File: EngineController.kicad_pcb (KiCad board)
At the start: 4 copper layers, 50 x 100 mm, 239 parts, among them IC1 TPS61089RNRR, IC2 AP2205-W5-7, IC3 AP2205-W5-7, IC4 TPS61089RNRR, J1 RBUS, J10 Conn_01x02_Male, J11 1053131104, J12 1053131104, J13 1053131104, J2 USB_C_Receptacle_USB2.0, J3 ServoCH1, J4 ServoCH2, J5 1053131104, J6 1053131104, J7 1053131104, J8 GPIO Breakout, J9 Micro_SD_Card_Det, Q1 SSM3K15AMFV,L3F, Q2 BUK9M11-40EX, U1 ESP32-S3, U2 SN65HVD230, U3 LM66200DRLR, U4 MAX77827AEFD+T, U5 SC4215, U6 SiC437BED-T1-GE3, U7 LTV-247, U8 ADS131M06IPBS, Y1 R940000171

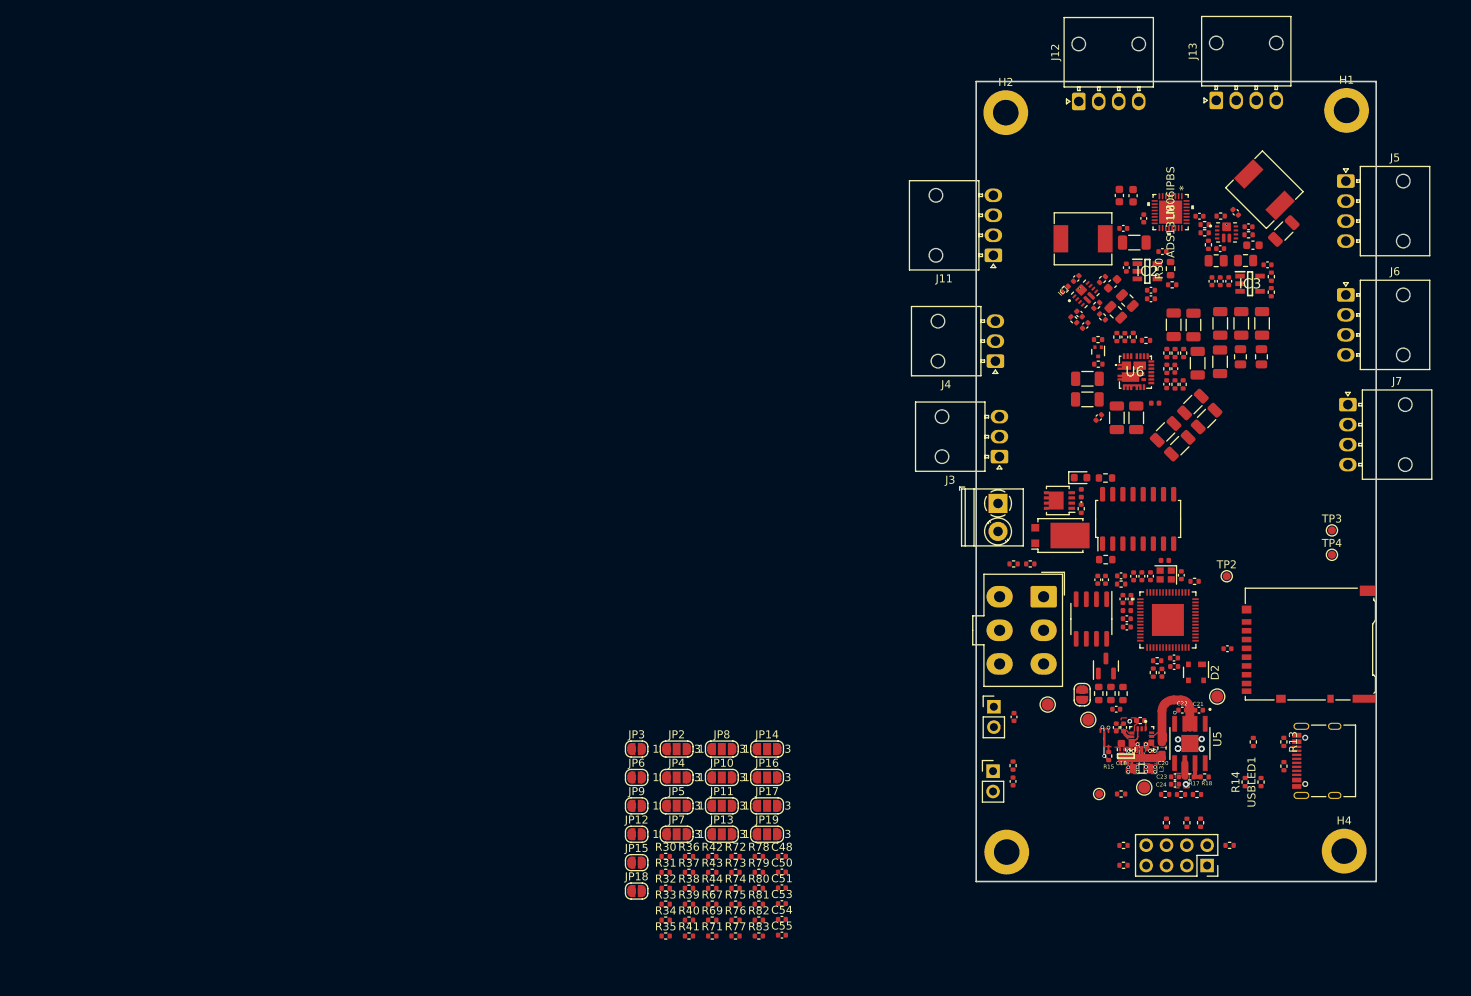
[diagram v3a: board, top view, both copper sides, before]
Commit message: Schematic done, components layed out, sensors wired up
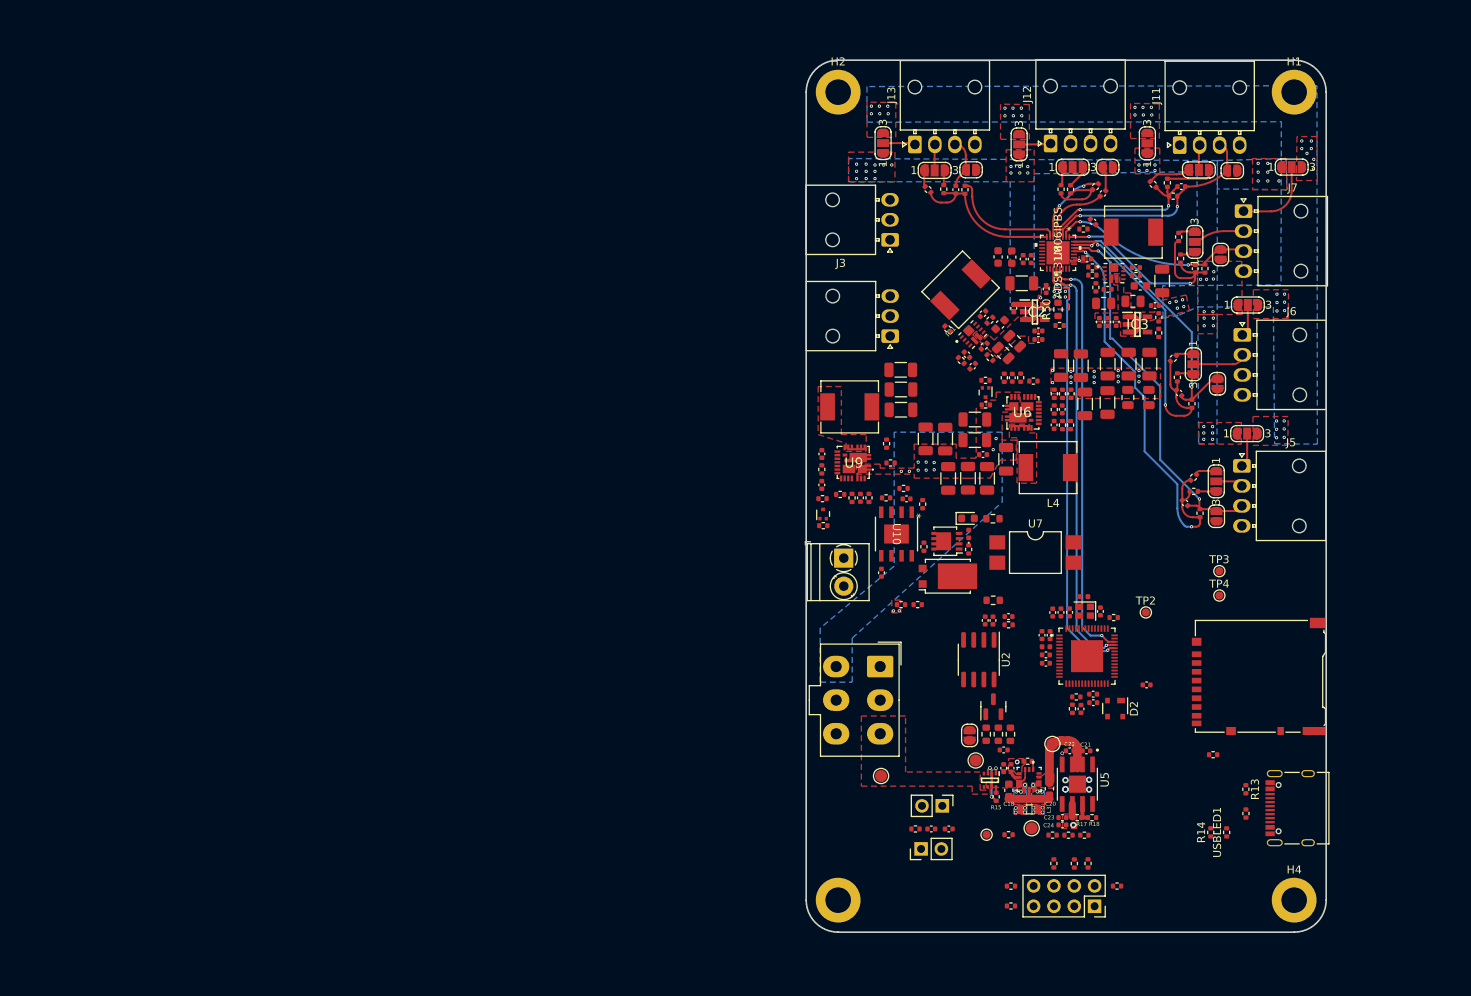
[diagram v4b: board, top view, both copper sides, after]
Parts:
- removed R71, R81, R82: 1k, Resistor_SMD:R_0402_1005Metric
- removed R80: 40.2k, Resistor_SMD:R_0402_1005Metric
- removed R83: 49k, Resistor_SMD:R_0402_1005Metric
- added C68: 1uF, Capacitor_SMD:C_0402_1005Metric, F.Cu at (137.9, 84.7)
- added C70: 4.7uF, Capacitor_SMD:C_0402_1005Metric, F.Cu at (137.9, 80.8)
- added C85: 47uF, Capacitor_SMD:C_1206_3216Metric, F.Cu at (147.8, 72.8)
- added C87: 47uF, Capacitor_SMD:C_1206_3216Metric, F.Cu at (147.8, 75.3)
- added C89: 47uF, Capacitor_SMD:C_1206_3216Metric, F.Cu at (147.7, 70.3)
- added C91: 0.1uF, Capacitor_SMD:C_0402_1005Metric, F.Cu at (142.7, 86.3)
- added C92: 2.2nF, Capacitor_SMD:C_0402_1005Metric, F.Cu at (148.5, 86.4)
- added C93: 100uF, Capacitor_SMD:C_0402_1005Metric, F.Cu at (145.3, 95.7)
- added L7: 3.3uH, iclr:IND_SRP6540-390M, F.Cu at (141.4, 74.9)
- added Q3: SSM3K15AMFV,L3F, Package_TO_SOT_SMD:SOT-723, F.Cu at (138.0, 88.3)
- added R52: 90k, Resistor_SMD:R_0402_1005Metric, F.Cu at (153.1, 47.7)
- added R53: 31.7k, Resistor_SMD:R_0402_1005Metric, F.Cu at (151.2, 47.8)
- added R54: 10k, Resistor_SMD:R_0402_1005Metric, F.Cu at (155.8, 47.8)
- added R57: 10k, Resistor_SMD:R_0402_1005Metric, F.Cu at (137.9, 82.7)
- added R58: 190k, Resistor_SMD:R_0402_1005Metric, F.Cu at (146.0, 79.5)
- added U10: TPS259621DDAT, EFuse:SO-PP-DDA-8_TEX, F.Cu at (147.2, 90.8)
- added U9: SiC437BED-T1-GE3, iclr:SiC437BEDT1GE3, F.Cu at (141.8, 81.9)
- C56: value 10uF -> 2.2uF
- C58: value 3.9nF -> 4.7nF
- L4: footprint Inductor_SMD:L_0402_1005Metric -> iclr:IND_SRP6540-390M
- R30: value 113k -> 90k
- R31: value 40.2k -> 31.7k
- R32, R38: value 1k -> 10k
- R33, R42: value 1k -> 90k
- R34: value 49k -> 31.7k
- R35, R67: value 113k -> 10k
- R36: value 40.2k -> 90k
- R37, R43: value 1k -> 31.7k
- R39: value 49k -> 90k
- R40: value 113k -> 31.7k
- R41, R75: value 40.2k -> 10k
- R44: value 49k -> 10k
- R45: value 7.87k -> 17.4k
- R46: value 360k -> 1K
- R47: value 100k -> 10k
- R48: value 560k -> 127k
- R51: value 309k -> 301k
- R56: value 360k -> 0k
- R69: value 40.2k -> 2.2
- R73: value 49k -> 200k
- R74: value 113k -> 100k
- R76: value 1k -> 464K
- R77: value 1k -> 33.2K
- R78: value 49k -> 47.5K
- R79: value 113k -> 453
- R85: value 953k -> 2k
- R86: value 118k -> 10k
- U7: footprint Package_SO:SOP-16_4.4x10.4mm_P1.27mm -> Package_DIP:SMDIP-4_W9.53mm
- moved JP12 111.5 mm to (189.2, 45.4), turned to 180 degrees
- moved R41 110.5 mm to (181.8, 48.6)
- moved R40 108.7 mm to (179.3, 47.1), turned to -45 degrees
- moved R39 108.2 mm to (181.1, 46.9), turned to -90 degrees
- moved JP15 105.0 mm to (173.6, 45.0), turned to 180 degrees
- moved JP10 104.4 mm to (196.6, 45.0)
- moved C53 102.6 mm to (182.8, 47.4)
- moved JP13 101.4 mm to (178.6, 42.0), turned to 90 degrees
- moved R38 100.8 mm to (185.8, 57.6), turned to 90 degrees
- moved JP9 100.4 mm to (187.7, 55.9), turned to 90 degrees
- moved R44 99.9 mm to (172.1, 47.4), turned to 45 degrees
- moved JP11 99.4 mm to (185.0, 45.3)
- moved JP18 99.4 mm to (156.5, 45.3), turned to 180 degrees
- moved C54 99.2 mm to (173.0, 48.2), turned to 45 degrees
- moved R36 98.7 mm to (182.5, 53.7), turned to -90 degrees
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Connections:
- net /Boosts/LDO11V_IN renamed /Boosts/LDO12V_IN
- C48 pad 1: /pressure_sensor/AIN3P -> /pressure_sensor/AIN0P
- C48 pad 2: /pressure_sensor/AIN3N -> /pressure_sensor/AIN0N
- C50 pad 1: /pressure_sensor/AIN4P -> /pressure_sensor/AIN1P
- C50 pad 2: /pressure_sensor/AIN4N -> /pressure_sensor/AIN1N
- C51 pad 1: /pressure_sensor/AIN5P -> /pressure_sensor/AIN2P
- C51 pad 2: /pressure_sensor/AIN5N -> /pressure_sensor/AIN2N
- C53 pad 1: /pressure_sensor/AIN0P -> /pressure_sensor/AIN3P
- C53 pad 2: /pressure_sensor/AIN0N -> /pressure_sensor/AIN3N
- C54 pad 1: /pressure_sensor/AIN2P -> /pressure_sensor/AIN4P
- C54 pad 2: /pressure_sensor/AIN2N -> /pressure_sensor/AIN4N
- C55 pad 1: /pressure_sensor/AIN1P -> /pressure_sensor/AIN5P
- C55 pad 2: /pressure_sensor/AIN1N -> /pressure_sensor/AIN5N
- C72 pad 2: Net-(U8-DVDD) -> +3V3
- C73 pad 1: /Boosts/10V -> +12V
- IC3 pad 5: /Boosts/10V -> +12V
- J10 pad 1: /Pyro/DeployPWR -> /Pyro/PyroV
- J6 pad 3: /pressure_sensor/AIN2N -> /pressure_sensor/AIN1N
- J7 pad 3: /pressure_sensor/AIN1N -> /pressure_sensor/AIN2N
- JP11 pad 3: /pressure_sensor/AIN3P -> Net-(JP11-B)
- JP14 pad 3: /pressure_sensor/AIN4P -> Net-(JP14-B)
- JP17 pad 3: /pressure_sensor/AIN5P -> Net-(JP17-B)
- JP2 pad 3: /pressure_sensor/AIN0P -> Net-(JP2-B)
- JP5 pad 3: /pressure_sensor/AIN2P -> Net-(JP5-B)
- JP6 pad 2: /pressure_sensor/AIN2N -> /pressure_sensor/AIN1N
- JP8 pad 3: /pressure_sensor/AIN1P -> Net-(JP8-B)
- JP9 pad 2: /pressure_sensor/AIN1N -> /pressure_sensor/AIN2N
- Q1 pad 1: /BUCK_EN -> /buckC/BUCKC_EN
- R24 pad 2: /BUCK_EN -> /buckC/BUCKC_EN
- R30 pad 1: Net-(R30-Pad1) -> Net-(JP2-B)
- R30 pad 2: Net-(R30-Pad2) -> /pressure_sensor/AIN0P
- R31 pad 1: Net-(R30-Pad2) -> Net-(JP2-A)
- R31 pad 2: Net-(R31-Pad2) -> /pressure_sensor/AIN0P
- R32 pad 1: Net-(R30-Pad1) -> /pressure_sensor/AIN0P
- R32 pad 2: /pressure_sensor/AIN0P -> /pressure_sensor/AIN0N
- R33 pad 1: Net-(R31-Pad2) -> Net-(JP5-B)
- R33 pad 2: Net-(JP2-A) -> /pressure_sensor/AIN1P
- R34 pad 1: /pressure_sensor/AIN0P -> Net-(JP5-A)
- R34 pad 2: /pressure_sensor/AIN0N -> /pressure_sensor/AIN1P
- R35 pad 1: Net-(R35-Pad1) -> /pressure_sensor/AIN1P
- R35 pad 2: Net-(R35-Pad2) -> /pressure_sensor/AIN1N
- R36 pad 1: Net-(R35-Pad2) -> Net-(JP8-B)
- R36 pad 2: Net-(R36-Pad2) -> /pressure_sensor/AIN2P
- R37 pad 1: Net-(R35-Pad1) -> Net-(JP8-A)
- R38 pad 1: Net-(R36-Pad2) -> /pressure_sensor/AIN2P
- R38 pad 2: Net-(JP5-A) -> /pressure_sensor/AIN2N
- R39 pad 1: /pressure_sensor/AIN2P -> Net-(JP11-B)
- R39 pad 2: /pressure_sensor/AIN2N -> /pressure_sensor/AIN3P
- R40 pad 1: Net-(R40-Pad1) -> Net-(JP11-A)
- R40 pad 2: Net-(R40-Pad2) -> /pressure_sensor/AIN3P
- R41 pad 1: Net-(R40-Pad2) -> /pressure_sensor/AIN3P
- R41 pad 2: Net-(R41-Pad2) -> /pressure_sensor/AIN3N
- R42 pad 1: Net-(R40-Pad1) -> Net-(JP14-B)
- R42 pad 2: /pressure_sensor/AIN1P -> /pressure_sensor/AIN4P
- R43 pad 1: Net-(R41-Pad2) -> Net-(JP14-A)
- R43 pad 2: Net-(JP8-A) -> /pressure_sensor/AIN4P
- R44 pad 1: /pressure_sensor/AIN1P -> /pressure_sensor/AIN4P
- R44 pad 2: /pressure_sensor/AIN1N -> /pressure_sensor/AIN4N
- R56 pad 2: /Boosts/10V -> +12V
- R67 pad 1: Net-(R67-Pad1) -> GND
- R67 pad 2: Net-(R67-Pad2) -> /Pyro/FB
- R69 pad 1: Net-(R67-Pad2) -> /Pyro/PHASE
- R69 pad 2: Net-(R69-Pad2) -> Net-(C91-Pad2)
- R72 pad 1: Net-(R69-Pad2) -> GND
- R72 pad 2: Net-(JP11-A) -> /Pyro/BUCKP_EN
- R73 pad 1: /pressure_sensor/AIN3P -> Net-(U9-MODE_2)
- R73 pad 2: /pressure_sensor/AIN3N -> /Pyro/VDD
- R74 pad 1: Net-(R74-Pad1) -> Net-(U9-_MODE_1)
- R74 pad 2: Net-(R74-Pad2) -> GND
- R75 pad 1: Net-(R74-Pad2) -> /Pyro/EN
- R75 pad 2: Net-(R75-Pad2) -> /Pyro/Vin
- R76 pad 1: Net-(R74-Pad1) -> Net-(U10-EN/UVLO)
- R76 pad 2: /pressure_sensor/AIN4P -> /Pyro/EFuse_In
- R77 pad 1: Net-(R75-Pad2) -> Net-(U10-OVLO/OVCSEL)
- R77 pad 2: Net-(JP14-A) -> Net-(U10-EN/UVLO)
- R78 pad 1: /pressure_sensor/AIN4P -> Net-(U10-OVLO/OVCSEL)
- R78 pad 2: /pressure_sensor/AIN4N -> GND
- R79 pad 2: Net-(R79-Pad2) -> Net-(U10-OVLO/OVCSEL)
- U1 pad 18: /BUCK_EN -> /BUCKC_EN
- U1 pad 19: unconnected-(U1-GPIO14/ADC2_CH3-Pad19) -> /BUCKP_EN
- U1 pad 31: /VSPI_MOSI -> /VSPI_SCLK
- U1 pad 32: /VSPI_SCLK -> /VSPI_MISO
- U1 pad 33: /VSPI_MISO -> /VSPI_MOSI
- U1 pad 38: /HSPI_MOSI -> /HSPI_SCLK
- U1 pad 39: /HSPI_SCLK -> /HSPI_MISO
- U1 pad 40: /HSPI_MISO -> /HSPI_MOSI
- U8 pad 19: /SCLK -> /HSPI_SCLK
- U8 pad 20: /MISO -> /HSPI_MISO
- U8 pad 21: /MOSI -> /HSPI_MOSI
- U8 pad 26: Net-(U8-DVDD) -> +3V3
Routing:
- net /HSPI_SCLK: track 0.00 -> 53.7 mm, vias 0 -> 2
- net /HSPI_MISO: track 0.00 -> 52.7 mm, vias 0 -> 2
- net /pressure_sensor/AIN0P: track 0.00 -> 51.9 mm, vias 0 -> 2
- net /HSPI_MOSI: track 0.00 -> 51.7 mm, vias 0 -> 2
- net /pressure_sensor/AIN0N: track 0.00 -> 48.5 mm, vias 0 -> 2
- net /pressure_sensor/AIN1P: track 0.00 -> 40.1 mm, vias 0 -> 2
- net /pressure_sensor/AIN1N: track 0.00 -> 34.0 mm, vias 0 -> 2
- net /pressure_sensor/AIN2P: track 0.00 -> 30.4 mm, vias 0 -> 2
- net /pressure_sensor/AIN3N: track 0.00 -> 28.9 mm, vias 0 -> 2
- net /pressure_sensor/AIN2N: track 0.00 -> 25.8 mm, vias 0 -> 2
- net /pressure_sensor/AIN3P: track 0.00 -> 22.0 mm, vias 0 -> 2
- net /pressure_sensor/AIN5N: track 0.00 -> 21.0 mm
- net /pressure_sensor/AIN5P: track 0.00 -> 20.2 mm
- net /pressure_sensor/AIN4P: track 0.00 -> 16.4 mm
- net /pressure_sensor/AIN4N: track 0.00 -> 13.0 mm, vias 0 -> 2
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- added copper zone on B.Cu, net +12V
- added copper zone on F.Cu, net +12V
- added copper zone on B.Cu, net +5V
- added copper zone on F.Cu, net +5V
- added copper zone on F.Cu, net +6V
- added copper zone on F.Cu, net /Boosts/LDO12V_IN
- added copper zone on F.Cu, net /Boosts/LDO5.5V_IN
- added copper zone on F.Cu, net /Pyro/SW
- added copper zone on F.Cu, net /buckC/SW
- added copper zone on F.Cu, net RBUS_uC_V
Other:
- board size 50 x 100 mm -> 65 x 109 mm

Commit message: Wired up more stuff
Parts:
- moved C46 44.0 mm to (165.5, 69.0), turned to 135 degrees
- moved R29 43.2 mm to (164.0, 68.3), turned to -135 degrees
- moved R28 43.2 mm to (164.7, 69.7), turned to -45 degrees
- moved TP1 18.3 mm to (176.5, 131.1)
- moved TP7 12.3 mm to (176.3, 128.3)
- moved C15 6.87 mm to (153.7, 105.7), turned to 180 degrees
- moved C14 6.80 mm to (153.7, 106.7), turned to 180 degrees
- moved TP2 5.23 mm to (173.8, 98.2)
- moved C64 4.64 mm to (158.4, 55.9)
- moved C47 4.61 mm to (182.9, 108.6), turned to 90 degrees
- moved 12VLED1 2.05 mm to (148.0, 98.8)
- moved R6 2.05 mm to (145.9, 98.8)
- moved TP3 1.64 mm to (186.7, 94.1)
- moved TP4 1.64 mm to (186.7, 97.2)
- moved C1 1.53 mm to (164.9, 105.8), turned to 180 degrees
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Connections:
- C1 pad 1: +3V3 -> +3.3V
- C10 pad 1: +3V3 -> +3.3V
- C11 pad 1: +3V3 -> +3.3V
- C14 pad 1: +3V3 -> +3.3V
- C15 pad 1: +3V3 -> +3.3V
- C23 pad 2: +3V3 -> +3.3V
- C24 pad 2: +3V3 -> +3.3V
- C4 pad 1: +3V3 -> +3.3V
- C47 pad 1: +3V3 -> +3.3V
- C49 pad 1: +3V3 -> +3.3V
- C5 pad 1: +3V3 -> +3.3V
- C52 pad 1: +3V3 -> +3.3V
- C64 pad 1: +3V3 -> +3.3V
- C65 pad 1: +3V3 -> +3.3V
- C7 pad 1: +3V3 -> +3.3V
- C71 pad 1: +3V3 -> +3.3V
- C72 pad 2: +3V3 -> +3.3V
- C81 pad 1: +3V3 -> +3.3V
- C82 pad 1: +3V3 -> +3.3V
- C9 pad 1: +3V3 -> +3.3V
- IC1 pad 9: +3V3 -> +3.3V
- IC4 pad 9: +3V3 -> +3.3V
- J8 pad 5: +3V3 -> +3.3V
- J9 pad 4: +3V3 -> +3.3V
- L1 pad 1: +3V3 -> +3.3V
- L5 pad 1: +3V3 -> +3.3V
- L6 pad 1: +3V3 -> +3.3V
- R1 pad 1: +3V3 -> +3.3V
- R17 pad 1: +3V3 -> +3.3V
- R2 pad 1: +3V3 -> +3.3V
- R3 pad 1: +3V3 -> +3.3V
- R4 pad 2: +3V3 -> +3.3V
- R59 pad 1: +3V3 -> +3.3V
- R60 pad 1: +3V3 -> +3.3V
- R61 pad 1: +3V3 -> +3.3V
- R62 pad 1: +3V3 -> +3.3V
- R63 pad 1: +3V3 -> +3.3V
- R64 pad 1: +3V3 -> +3.3V
- R66 pad 1: +3V3 -> +3.3V
- TP7 pad 1: +3V3 -> +3.3V
- U1 pad 10: /GPIO5 -> /actuators/GPIO5
- U1 pad 11: /GPIO3 -> /actuators/GPIO3
- U1 pad 12: /GPIO1 -> /actuators/GPIO1
- U1 pad 13: /GPIO2 -> /actuators/GPIO2
- U1 pad 14: /GPIO0 -> /actuators/GPIO0
- U1 pad 18: /BUCKC_EN -> /buckC/BUCKC_EN
- U1 pad 20: +3V3 -> +3.3V
- U1 pad 31: /VSPI_SCLK -> /microSD/VSPI_MISO
- U1 pad 32: /VSPI_MISO -> /microSD/VSPI_SCLK
- U1 pad 46: +3V3 -> +3.3V
- U1 pad 55: +3V3 -> +3.3V
- U1 pad 56: +3V3 -> +3.3V
- U1 pad 9: /GPIO4 -> /actuators/GPIO4
- U2 pad 3: +3V3 -> +3.3V
- U5 pad 6: +3V3 -> +3.3V
- U7 pad 16: +3V3 -> +3.3V
- U8 pad 15: +3V3 -> +3.3V
- U8 pad 26: +3V3 -> +3.3V
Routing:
- net /Servo1PWM: track 0.00 -> 84.9 mm, vias 0 -> 4
- net /Servo2PWM: track 0.00 -> 66.6 mm, vias 0 -> 4
- net /ServoV_LOG: track 0.00 -> 52.9 mm, vias 0 -> 4
- net /BOOT: track 0.00 -> 42.5 mm, vias 0 -> 4
- net /CHIP_PU: track 0.00 -> 40.1 mm, vias 0 -> 4
- net /actuators/GPIO4: track 0.00 -> 38.2 mm, vias 0 -> 1
- net /actuators/GPIO1: track 0.00 -> 37.6 mm, vias 0 -> 1
- net /actuators/GPIO3: track 0.00 -> 35.0 mm, vias 0 -> 1
- net /actuators/GPIO5: track 0.00 -> 34.8 mm, vias 0 -> 1
- net /actuators/GPIO2: track 0.00 -> 33.7 mm, vias 0 -> 1
- net /BuckPGOOD: track 0.00 -> 32.2 mm
- net /Data+: track 0.00 -> 31.7 mm
- net /actuators/GPIO0: track 0.00 -> 31.5 mm, vias 0 -> 1
- net VBUS: track 5.27 -> 36.8 mm
- net /Data-: track 0.00 -> 31.5 mm
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- added copper zone on F.Cu, net +3.3V
- added copper zone on B.Cu, net +6V
- added copper zone on F.Cu, net /Pyro/EFuse_In
- removed copper zone on F.Cu, net +3V3
